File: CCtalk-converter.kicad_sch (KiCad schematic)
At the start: 0 parts

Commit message: latest updates
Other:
- sheet S1U2-to-CCtalk-converter1 renamed S1U2-to-CCtalk-converter
- sheet S1U2-to-CCtalk-converter: file USB-C-to-CCtalk-converter/USB-C-to-CCtalk-converter.kicad_sch -> S1U2-to-CCtalk-converter/S1U2-to-CCtalk-converter.kicad_sch

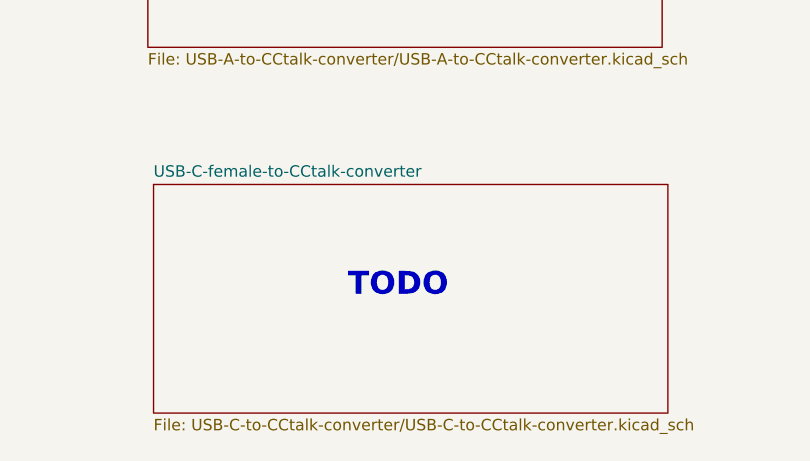
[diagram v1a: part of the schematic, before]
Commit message: add s1u2 dxf bckg and place components
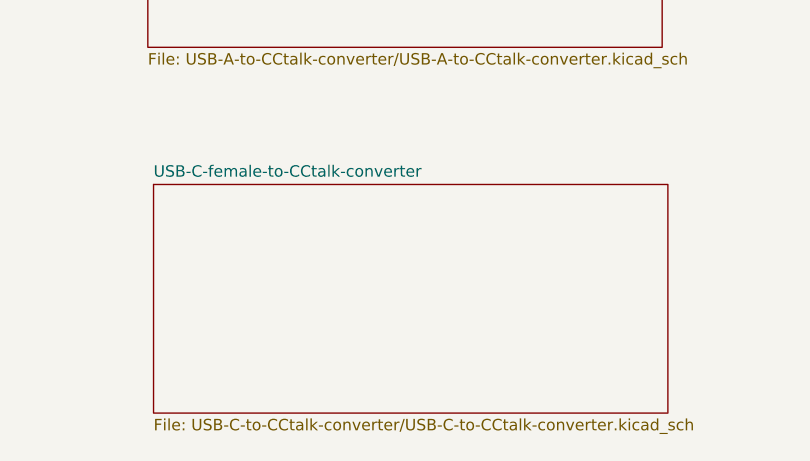
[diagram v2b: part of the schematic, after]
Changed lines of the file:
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@@
     (rev "v0.1")
-  )
-  (text "TODO" (at 151.13 128.27 0)
-    (effects (font (size 2.54 2.54) (thickness 0.508) bold) (justify left bottom))
   )
   (text "TODO" (at 223.52 130.175 0)
